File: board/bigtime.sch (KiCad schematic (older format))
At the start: 58 parts, among them IC1 NPIC6C596A, IC2 TPS62152, IC3 25AA02E48, IC4 STM32F407VET6, J2 MICROUSB, P1 CONN_IN, P2 CONN_OUT, P3 +12V, P4 SWD_TC, P5 SWD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

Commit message: Specced part for brightness trimpot
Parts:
- added R30, R31: 33, agg:0603, symbol R_Small
- RV1: footprint (none) -> footprints:3386P; Farnell (none) -> 9355049
- TP1, TP2: symbol TEST -> TEST-RESCUE-bigtime
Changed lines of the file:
@@
 $EndComp
 $Comp
-L GND #PWR01
+L GND #PWR29
 U 1 1 58AB653E
 P 8950 3500
-F 0 "#PWR01" H 5750 2050 50  0001 C CNN
+F 0 "#PWR29" H 5750 2050 50  0001 C CNN
 F 1 "GND" H 8955 3327 50  0000 C CNN
 F 2 "" H 5750 2300 50  0000 C CNN
@@
 $EndComp
 $Comp
-L GND #PWR02
+L GND #PWR34
 U 1 1 58AB65DB
 P 9850 3500
-F 0 "#PWR02" H 5900 1600 50  0001 C CNN
+F 0 "#PWR34" H 5900 1600 50  0001 C CNN
 F 1 "GND" H 9855 3327 50  0000 C CNN
 F 2 "" H 5900 1850 50  0000 C CNN
@@
 STCP
 $Comp
-L +3V3 #PWR03
+L +3V3 #PWR31
 U 1 1 58AB6B00
 P 9500 2950
-F 0 "#PWR03" H 5850 1800 50  0001 C CNN
+F 0 "#PWR31" H 5850 1800 50  0001 C CNN
 F 1 "+3V3" H 9515 3123 50  0000 C CNN
 F 2 "" H 5850 1950 50  0000 C CNN
@@
 $EndComp
 $Comp
-L +12V #PWR04
+L +12V #PWR22
 U 1 1 58AB6FA8
 P 8100 900
-F 0 "#PWR04" H 1500 -500 50  0001 C CNN
+F 0 "#PWR22" H 1500 -500 50  0001 C CNN
 F 1 "+12V" H 8115 1073 50  0000 C CNN
 F 2 "" H 1500 -350 50  0000 C CNN
@@
 $EndComp
 $Comp
-L GND #PWR05
+L GND #PWR23
 U 1 1 58AB7079
 P 8100 1550
-F 0 "#PWR05" H 1900 -50 50  0001 C CNN
+F 0 "#PWR23" H 1900 -50 50  0001 C CNN
 F 1 "GND" H 8105 1377 50  0000 C CNN
 F 2 "" H 1900 200 50  0000 C CNN
@@
 $EndComp
 $Comp
-L GND #PWR06
+L GND #PWR28
 U 1 1 58AB711C
 P 8600 2300
-F 0 "#PWR06" H 2250 -350 50  0001 C CNN
+F 0 "#PWR28" H 2250 -350 50  0001 C CNN
 F 1 "GND" H 8605 2127 50  0000 C CNN
 F 2 "" H 2250 -100 50  0000 C CNN
@@
 $EndComp
 $Comp
-L GND #PWR07
+L GND #PWR33
 U 1 1 58AB72DE
 P 9600 1800
-F 0 "#PWR07" H 2100 -200 50  0001 C CNN
+F 0 "#PWR33" H 2100 -200 50  0001 C CNN
 F 1 "GND" H 9605 1627 50  0000 C CNN
 F 2 "" H 2100 50  50  0000 C CNN
@@
 $EndComp
 $Comp
-L +3V3 #PWR08
+L +3V3 #PWR36
 U 1 1 58AB765A
 P 10950 950
-F 0 "#PWR08" H 11000 1000 50  0001 C CNN
+F 0 "#PWR36" H 11000 1000 50  0001 C CNN
 F 1 "+3V3" H 10965 1123 50  0000 C CNN
 F 2 "" H 2150 -150 50  0000 C CNN
@@
 $EndComp
 $Comp
-L GND #PWR09
+L GND #PWR35
 U 1 1 58AB76DE
 P 10450 1300
-F 0 "#PWR09" H 2350 -500 50  0001 C CNN
+F 0 "#PWR35" H 2350 -500 50  0001 C CNN
 F 1 "GND" H 10455 1127 50  0000 C CNN
 F 2 "" H 2350 -250 50  0000 C CNN
@@
 $EndComp
 $Comp
-L GND #PWR010
+L GND #PWR21
 U 1 1 58AB81EC
 P 7650 5450
-F 0 "#PWR010" H 3250 150 50  0001 C CNN
+F 0 "#PWR21" H 3250 150 50  0001 C CNN
 F 1 "GND" H 7655 5277 50  0000 C CNN
 F 2 "" H 3250 400 50  0000 C CNN
@@
 $EndComp
 $Comp
-L +3V3 #PWR011
+L +3V3 #PWR20
 U 1 1 58AB83D7
 P 7650 5150
-F 0 "#PWR011" H 3200 350 50  0001 C CNN
+F 0 "#PWR20" H 3200 350 50  0001 C CNN
 F 1 "+3V3" H 7665 5323 50  0000 C CNN
 F 2 "" H 3200 500 50  0000 C CNN
@@
 $EndComp
 $Comp
-L +12V #PWR012
+L +12V #PWR26
 U 1 1 58B71B7B
 P 8350 4000
-F 0 "#PWR012" H 8400 4050 50  0001 C CNN
+F 0 "#PWR26" H 8400 4050 50  0001 C CNN
 F 1 "+12V" H 8365 4173 50  0000 C CNN
 F 2 "" H 250 100 50  0001 C CNN
@@
 $EndComp
 $Comp
-L GND #PWR013
+L GND #PWR27
 U 1 1 58B72373
 P 8350 4400
-F 0 "#PWR013" H 8400 4450 50  0001 C CNN
+F 0 "#PWR27" H 8400 4450 50  0001 C CNN
 F 1 "GND" H 8355 4227 50  0000 C CNN
 F 2 "" H 800 250 50  0001 C CNN
@@
 $EndComp
 $Comp
-L GND #PWR014
+L GND #PWR30
 U 1 1 58B72502
 P 9250 4350
-F 0 "#PWR014" H 9300 4400 50  0001 C CNN
+F 0 "#PWR30" H 9300 4400 50  0001 C CNN
 F 1 "GND" H 9255 4177 50  0001 C CNN
 F 2 "" H 800 350 50  0001 C CNN
@@
 F 0 "RV1" H 9480 4454 50  0000 R CNN
 F 1 "100k" H 9480 4545 50  0000 R CNN
-F 2 "" H 850 800 50  0001 C CNN
-F 3 "" H 850 800 50  0001 C CNN
+F 2 "footprints:3386P" H 850 800 50  0001 C CNN
+F 3 "http://www.farnell.com/datasheets/2061252.pdf" H 850 800 50  0001 C CNN
+F 4 "9355049" H 9550 4500 60  0001 C CNN "Farnell"
 	1    9550 4500
 	-1   0    0    1
@@
 $EndComp
 $Comp
-L GND #PWR015
+L GND #PWR32
 U 1 1 58B7299B
 P 9550 4950
-F 0 "#PWR015" H 9600 5000 50  0001 C CNN
+F 0 "#PWR32" H 9600 5000 50  0001 C CNN
 F 1 "GND" H 9555 4777 50  0000 C CNN
 F 2 "" H 450 1100 50  0001 C CNN
@@
 $EndComp
 $Comp
-L GND #PWR016
+L GND #PWR25
 U 1 1 58BC5CDB
 P 8100 3050
-F 0 "#PWR016" H 8100 2800 50  0001 C CNN
+F 0 "#PWR25" H 8100 2800 50  0001 C CNN
 F 1 "GND" V 8050 2850 50  0000 C CNN
 F 2 "" H 8100 3050 50  0000 C CNN
@@
 $EndComp
 $Comp
-L +12V #PWR017
+L +12V #PWR24
 U 1 1 58BC5F20
 P 8100 2950
-F 0 "#PWR017" H 8100 2800 50  0001 C CNN
+F 0 "#PWR24" H 8100 2800 50  0001 C CNN
 F 1 "+12V" V 8050 3150 50  0000 C CNN
 F 2 "" H 8100 2950 50  0000 C CNN
@@
 $EndComp
 $Comp
-L +3V3 #PWR018
+L +3V3 #PWR2
 U 1 1 58BDC70F
 P 1200 750
-F 0 "#PWR018" H 1200 600 50  0001 C CNN
+F 0 "#PWR2" H 1200 600 50  0001 C CNN
 F 1 "+3V3" H 1215 923 50  0000 C CNN
 F 2 "" H 1200 750 50  0000 C CNN
@@
 $EndComp
 $Comp
-L GND #PWR019
+L GND #PWR3
 U 1 1 58BDC8A3
 P 1200 1050
-F 0 "#PWR019" H 1200 800 50  0001 C CNN
+F 0 "#PWR3" H 1200 800 50  0001 C CNN
 F 1 "GND" H 1205 877 50  0000 C CNN
 F 2 "" H 1200 1050 50  0000 C CNN
@@
 $EndComp
 $Comp
-L +3V3 #PWR020
+L +3V3 #PWR10
 U 1 1 58BDED17
 P 2450 1450
-F 0 "#PWR020" H 2450 1300 50  0001 C CNN
+F 0 "#PWR10" H 2450 1300 50  0001 C CNN
 F 1 "+3V3" H 2465 1623 50  0000 C CNN
 F 2 "" H 2450 1450 50  0000 C CNN
@@
 Connection ~ 2450 2950
 $Comp
-L GND #PWR021
+L GND #PWR9
 U 1 1 58BE0492
 P 2350 3300
-F 0 "#PWR021" H 2350 3050 50  0001 C CNN
+F 0 "#PWR9" H 2350 3050 50  0001 C CNN
 F 1 "GND" H 2355 3127 50  0000 C CNN
 F 2 "" H 2350 3300 50  0000 C CNN
@@
 	1750 2550 2550 2550
 $Comp
-L GND #PWR022
+L GND #PWR6
 U 1 1 58BE1218
 P 1750 3100
-F 0 "#PWR022" H 1750 2850 50  0001 C CNN
+F 0 "#PWR6" H 1750 2850 50  0001 C CNN
 F 1 "GND" H 1755 2927 50  0000 C CNN
 F 2 "" H 1750 3100 50  0000 C CNN
@@
 $EndComp
 $Comp
-L GND #PWR023
+L GND #PWR8
 U 1 1 58BE1307
 P 2000 3100
-F 0 "#PWR023" H 2000 2850 50  0001 C CNN
+F 0 "#PWR8" H 2000 2850 50  0001 C CNN
 F 1 "GND" H 2005 2927 50  0000 C CNN
 F 2 "" H 2000 3100 50  0000 C CNN
@@
 $EndComp
 $Comp
-L GND #PWR024
+L GND #PWR1
 U 1 1 58BE2016
 P 900 3850
-F 0 "#PWR024" H 900 3600 50  0001 C CNN
+F 0 "#PWR1" H 900 3600 50  0001 C CNN
 F 1 "GND" H 905 3677 50  0000 C CNN
 F 2 "" H 900 3850 50  0000 C CNN
@@
 Connection ~ 1900 3850
 $Comp
-L GND #PWR025
+L GND #PWR5
 U 1 1 58BE546E
 P 1650 4250
-F 0 "#PWR025" H 1650 4000 50  0001 C CNN
+F 0 "#PWR5" H 1650 4000 50  0001 C CNN
 F 1 "GND" H 1655 4077 50  0000 C CNN
 F 2 "" H 1650 4250 50  0000 C CNN
@@
 $EndComp
 $Comp
-L GND #PWR026
+L GND #PWR7
 U 1 1 58BE57D1
 P 1900 4250
-F 0 "#PWR026" H 1900 4000 50  0001 C CNN
+F 0 "#PWR7" H 1900 4000 50  0001 C CNN
 F 1 "GND" H 1905 4077 50  0000 C CNN
 F 2 "" H 1900 4250 50  0000 C CNN
@@
 $EndComp
 $Comp
-L GND #PWR027
+L GND #PWR4
 U 1 1 58BE58CC
 P 1350 3950
-F 0 "#PWR027" H 1350 3700 50  0001 C CNN
+F 0 "#PWR4" H 1350 3700 50  0001 C CNN
 F 1 "GND" H 1355 3777 50  0000 C CNN
 F 2 "" H 1350 3950 50  0000 C CNN
@@
 NoConn ~ 6400 7450
 $Comp
-L GND #PWR028
+L GND #PWR16
 U 1 1 58BED3C9
 P 5500 6800
-F 0 "#PWR028" H 5500 6550 50  0001 C CNN
+F 0 "#PWR16" H 5500 6550 50  0001 C CNN
 F 1 "GND" H 5505 6627 50  0000 C CNN
 F 2 "" H 5500 6800 50  0000 C CNN
@@
 $EndComp
 $Comp
-L GND #PWR029
+L GND #PWR14
 U 1 1 58BED4CA
 P 5300 7550
-F 0 "#PWR029" H 5300 7300 50  0001 C CNN
+F 0 "#PWR14" H 5300 7300 50  0001 C CNN
 F 1 "GND" H 5305 7377 50  0000 C CNN
 F 2 "" H 5300 7550 50  0000 C CNN
@@
 	5400 7250 5300 7250
 $Comp
-L +3V3 #PWR030
+L +3V3 #PWR13
 U 1 1 58BEDD12
 P 5250 7150
-F 0 "#PWR030" H 5250 7000 50  0001 C CNN
+F 0 "#PWR13" H 5250 7000 50  0001 C CNN
 F 1 "+3V3" H 5265 7323 50  0000 C CNN
 F 2 "" H 5250 7150 50  0000 C CNN
@@
 	5250 7150 5400 7150
 $Comp
-L +3V3 #PWR031
+L +3V3 #PWR15
 U 1 1 58BEE50F
 P 5400 6550
-F 0 "#PWR031" H 5400 6400 50  0001 C CNN
+F 0 "#PWR15" H 5400 6400 50  0001 C CNN
 F 1 "+3V3" H 5415 6723 50  0000 C CNN
 F 2 "" H 5400 6550 50  0000 C CNN
@@
 	5850 4150 5850 4050
 $Comp
-L +3V3 #PWR032
+L +3V3 #PWR17
 U 1 1 58BFD9B9
 P 5600 3850
-F 0 "#PWR032" H 5600 3700 50  0001 C CNN
+F 0 "#PWR17" H 5600 3700 50  0001 C CNN
 F 1 "+3V3" H 5615 4023 50  0000 C CNN
 F 2 "" H 5600 3850 50  0000 C CNN
@@
 Connection ~ 5600 3850
 $Comp
-L GND #PWR033
+L GND #PWR18
 U 1 1 58BFDAC2
 P 5600 4150
-F 0 "#PWR033" H 5600 3900 50  0001 C CNN
+F 0 "#PWR18" H 5600 3900 50  0001 C CNN
 F 1 "GND" H 5605 3977 50  0000 C CNN
 F 2 "" H 5600 4150 50  0000 C CNN
@@
 $EndComp
 $Comp
-L GND #PWR034
+L GND #PWR11
 U 1 1 58D5CD9D
 P 4100 3500
-F 0 "#PWR034" H 4100 3250 50  0001 C CNN
+F 0 "#PWR11" H 4100 3250 50  0001 C CNN
 F 1 "GND" H 4105 3327 50  0000 C CNN
 F 2 "" H 4100 3500 50  0001 C CNN
@@
 $EndComp
 $Comp
-L GND #PWR035
+L GND #PWR12
 U 1 1 58D5CE67
 P 4350 3500
-F 0 "#PWR035" H 4350 3250 50  0001 C CNN
+F 0 "#PWR12" H 4350 3250 50  0001 C CNN
 F 1 "GND" H 4355 3327 50  0000 C CNN
 F 2 "" H 4350 3500 50  0001 C CNN
@@
 USB_D+
 $Comp
-L GND #PWR036
+L GND #PWR19
 U 1 1 58D582F5
 P 6300 1700
-F 0 "#PWR036" H 6300 1450 50  0001 C CNN
+F 0 "#PWR19" H 6300 1450 50  0001 C CNN
 F 1 "GND" H 6305 1527 50  0000 C CNN
 F 2 "" H 6300 1700 50  0001 C CNN
@@
 	6150 1150 6550 1150
 $Comp
-L TEST TP1
+L TEST-RESCUE-bigtime TP1
 U 1 1 58D6D0D0
 P 10550 900
@@
 Connection ~ 10550 1000
 $Comp
-L TEST TP2
+L TEST-RESCUE-bigtime TP2
 U 1 1 58D706B5
 P 1200 3450
@@
 	1200 3450 1200 3550
 Connection ~ 1200 3550
+$Comp
+L R_Small R30
+U 1 1 58D9B0C5
+P 4600 5600
+F 0 "R30" V 4550 5750 50  0000 C CNN
+F 1 "33" V 4600 5600 50  0000 C CNN
+F 2 "agg:0603" H 4600 5600 50  0001 C CNN
+F 3 "" H 4600 5600 50  0000 C CNN
+	1    4600 5600
+	0    1    1    0
+$EndComp
+$Comp
+L R_Small R31
+U 1 1 58D9B8C8
+P 4600 5700
+F 0 "R31" V 4550 5850 50  0000 C CNN
+F 1 "33" V 4600 5700 50  0000 C CNN
+F 2 "agg:0603" H 4600 5700 50  0001 C CNN
+F 3 "" H 4600 5700 50  0000 C CNN
+	1    4600 5700
+	0    1    1    0
+$EndComp
 $EndSCHEMATC

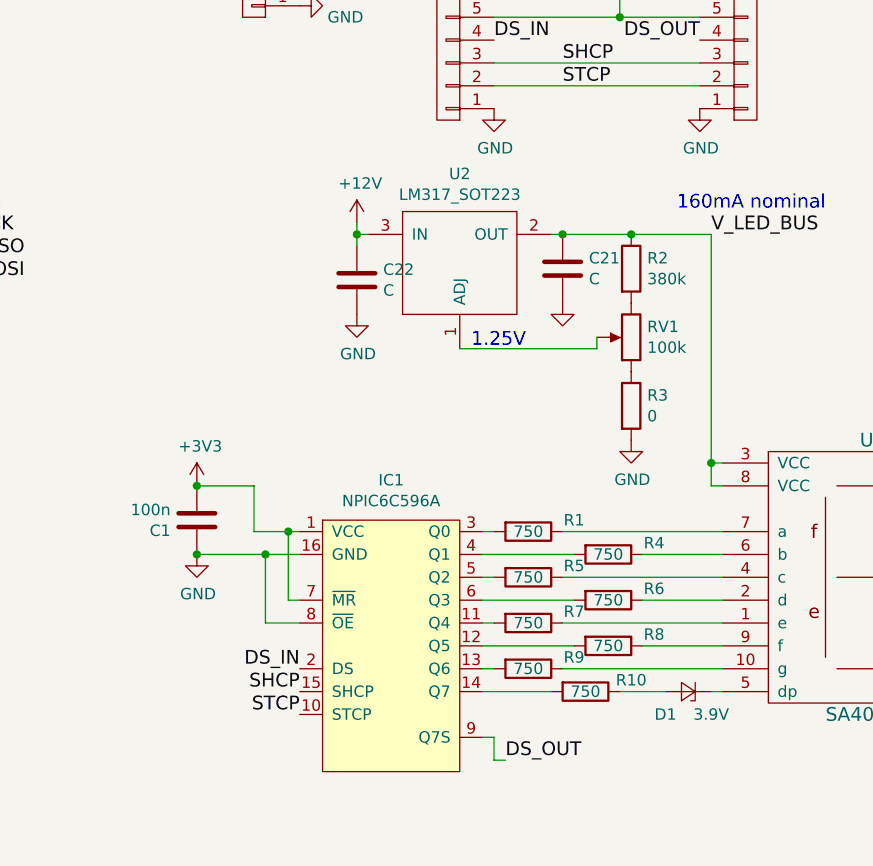
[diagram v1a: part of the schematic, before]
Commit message: New LDO, new dimmer network, zener
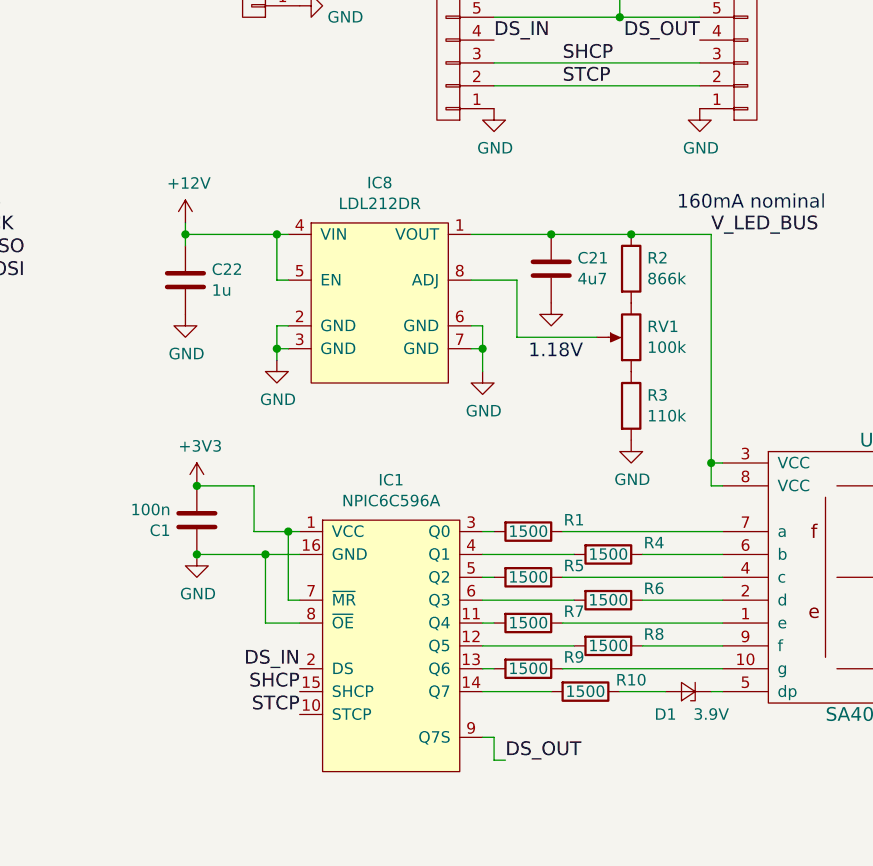
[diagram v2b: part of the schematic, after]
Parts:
- removed U2: LM317_SOT223, symbol LM317_SOT223
- added IC8: LDL212DR, agg:SOIC-8, symbol LDL212DR
- C21: value C -> 4u7
- C22: value C -> 1u
- D1: footprint (none) -> agg:SOD-323; Farnell (none) -> 8735662
- R1, R10, R4, R5, R6, R7, R8, R9: value 750 -> 1500; Farnell (none) -> 9233407
- R2: value 380k -> 866k; Farnell (none) -> 2303318
- R3: value 0 -> 110k; Farnell (none) -> 2502402
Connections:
- net +12V: now also IC8.4 (VIN), IC8.5 (EN)
- net GND: now also IC8.2 (GND), IC8.3 (GND), IC8.6 (GND), IC8.7 (GND)
- net V_LED_BUS: now also IC8.1 (VOUT)
- net at RV1.2: now also IC8.8 (ADJ)
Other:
- note added: "1.18V"
- note removed: "1.25V"
- moved on the sheet: C21, C22

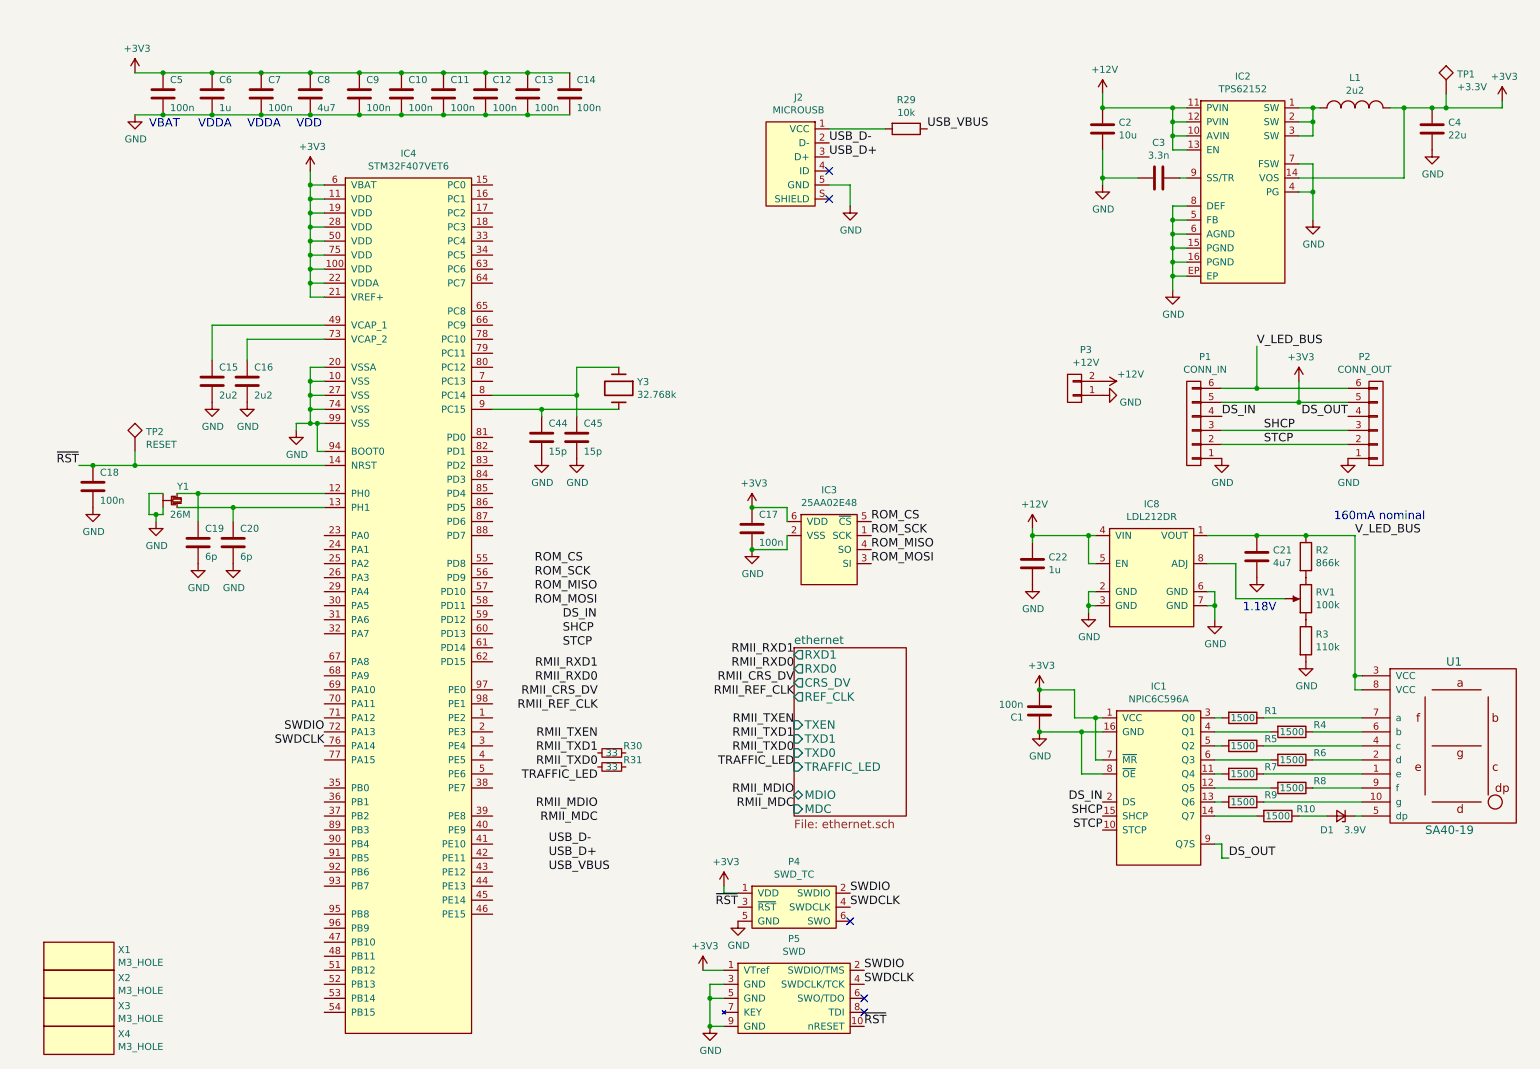
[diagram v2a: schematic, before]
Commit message: Rough first go at placement minus some shrapnel
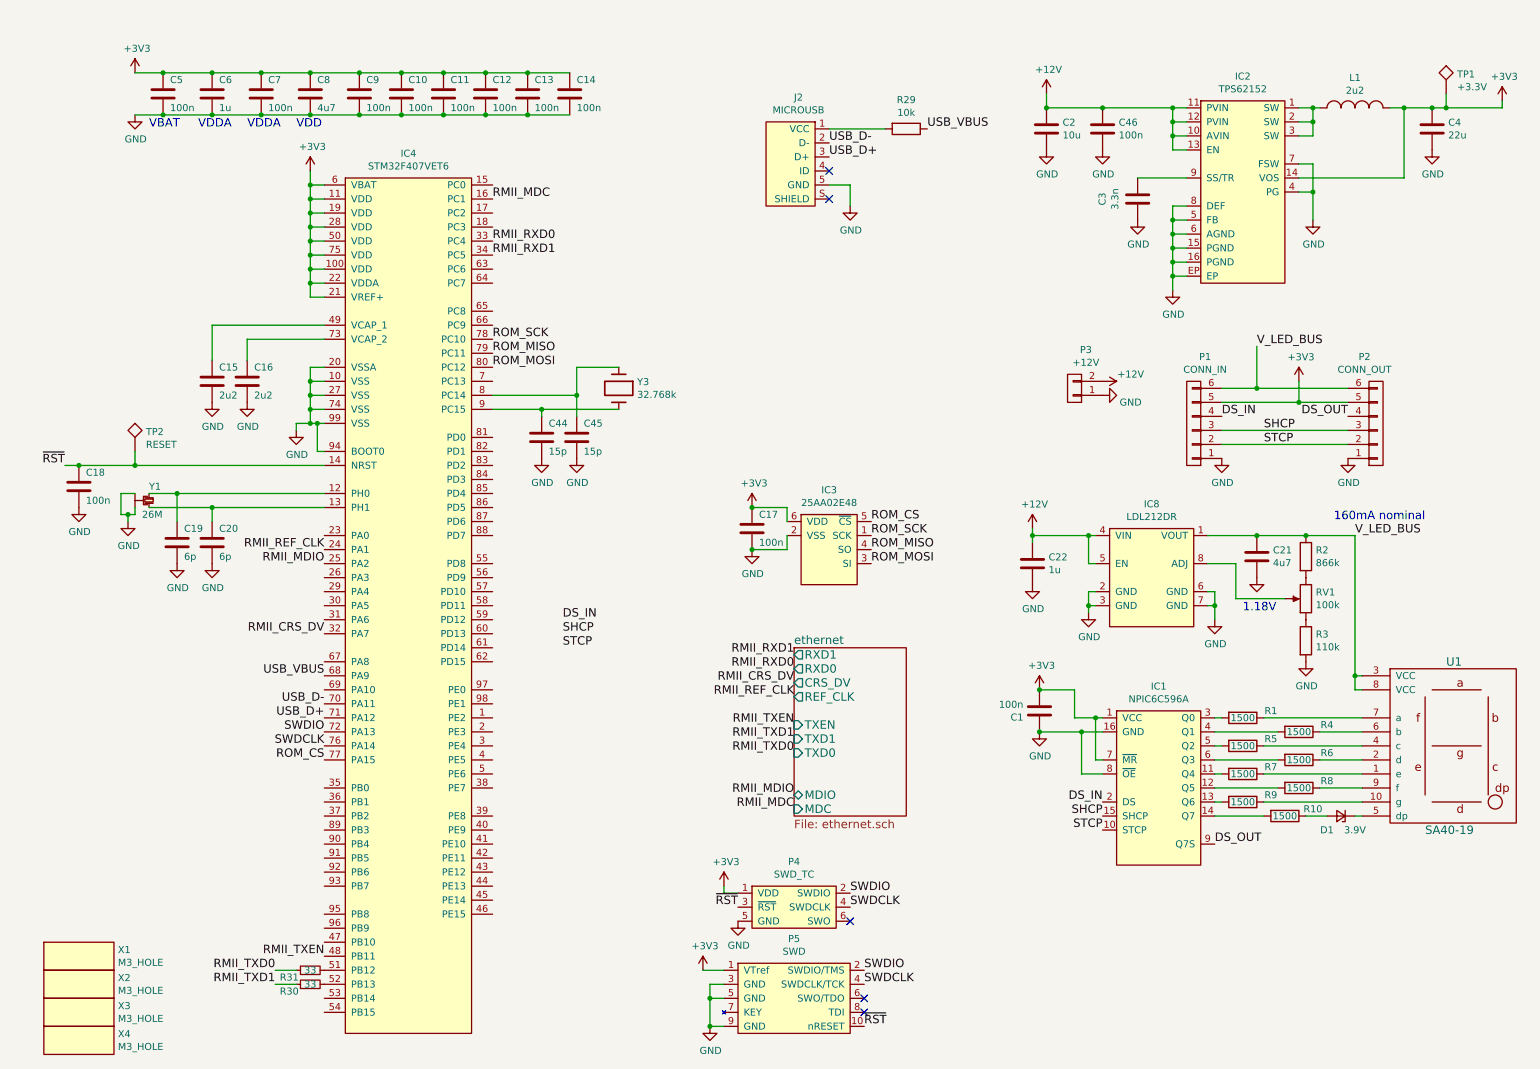
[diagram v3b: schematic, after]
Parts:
- added C46: 100n, agg:0603, symbol C
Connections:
- net +12V: now also C46.1
- net GND: now also C46.2
- net RMII_CRS_DV: now also IC4.32 (PA7)
- net RMII_MDC: now also IC4.16 (PC1)
- net RMII_MDIO: now also IC4.25 (PA2)
- net RMII_REF_CLK: now also IC4.24 (PA1)
- net RMII_RXD0: now also IC4.33 (PC4)
- net RMII_RXD1: now also IC4.34 (PC5)
- net RMII_TXD0: now also R31.1; no longer R31.2
- net RMII_TXD1: now also R30.1; no longer R30.2
- net RMII_TXEN: now also IC4.48 (PB11)
- net ROM_CS: now also IC4.77 (PA15)
- net ROM_MISO: now also IC4.79 (PC11)
- net ROM_MOSI: now also IC4.80 (PC12)
- net ROM_SCK: now also IC4.78 (PC10)
- net USB_D+: now also IC4.71 (PA12)
- net USB_D-: now also IC4.70 (PA11)
- net USB_VBUS: now also IC4.68 (PA9)
- net at IC4.51 (PB12): now also R31.2
- net at IC4.52 (PB13): now also R30.2
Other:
- moved on the sheet: C18, C19, C2, C20, C3, R10, R30, R31, R4, R6, R8, Y1
